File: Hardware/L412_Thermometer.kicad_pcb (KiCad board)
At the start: 2 copper layers, 45 x 45 mm, 21 parts, among them J1 USB_B_Mini, J2 Conn_01x03, J3 Conn_Si7021, J4 Conn_LCD, J5 Debug, J6 Serial, Q1 BSS84AKW, U1 AP7343D-33W5, U2 STM32L412KBTx, Y1 ABS07 [9pF, 32.768kHz]

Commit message: PCB updated
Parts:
- added C10: 100n, Capacitor_SMD:C_0603_1608Metric, F.Cu at (170.2, 105.4)
- added C8: C, Capacitor_SMD:C_0603_1608Metric, F.Cu at (139.7, 93.7)
- added C9: 100n, Capacitor_SMD:C_0603_1608Metric, F.Cu at (170.2, 93.0)
- added SW1: SW_Push, Button_Switch_THT:SW_PUSH_6mm, F.Cu at (172.5, 90.7)
- added SW2: SW_Push, Button_Switch_THT:SW_PUSH_6mm, F.Cu at (172.5, 103.2)
- J1: moved to B.Cu
- J2: value Conn_01x03 -> Power
- J3: value Conn_Si7021 -> Si7021
- J4, J5: moved to F.Cu
- moved J3 47.2 mm to (172.1, 84.5), turned to 90 degrees
- moved J2 39.4 mm to (131.8, 83.8), turned to 180 degrees
- moved J6 28.6 mm to (131.8, 100.1), turned to 180 degrees
- moved C4 27.4 mm to (135.6, 83.1), turned to -90 degrees
- moved U1 25.5 mm to (138.2, 83.4), turned to -90 degrees
- moved C5 25.4 mm to (140.7, 83.1), turned to -90 degrees
- moved J4 18.0 mm to (154.7, 113.1)
- moved J1 16.6 mm to (177.7, 76.7), turned to -90 degrees
- moved C3 15.9 mm to (144.5, 85.8)
- moved R1 13.0 mm to (152.1, 108.2), turned to 90 degrees
- moved J5 5.57 mm to (151.9, 76.5)
- moved C1 5.48 mm to (146.1, 85.9)
- moved U2 5.43 mm to (150.6, 90.7)
- moved C2 5.39 mm to (155.2, 95.5)
- moved C6 5.29 mm to (140.4, 88.4)
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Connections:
- Q1 pad 1: BAT_MEAS -> BAT_MEAS_EN
- R2 pad 2: BAT_MEAS -> BAT_MEAS_EN
- R3 pad 2: VBAT -> V_BAT
- R4 pad 1: VBAT -> V_BAT
- U2 pad 29: unconnected-(U2-Pad29) -> BAT_MEAS_EN
- U2 pad 30: unconnected-(U2-Pad30) -> SCREEN
- U2 pad 6: VBAT -> WKUP
- U2 pad 7: BAT_MEAS -> V_BAT
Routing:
- net +3V3: track 61.8 -> 0.00 mm, vias 1 -> 0
- net +BATT: track 40.6 -> 0.00 mm, vias 1 -> 0
- net Net-(J3-Pad4): track 29.3 -> 0.00 mm, vias 1 -> 0
- net Net-(J3-Pad3): track 27.4 -> 0.00 mm, vias 1 -> 0
- net NRST: track 24.6 -> 0.00 mm, vias 1 -> 0
- net LCD_CE: track 23.0 -> 0.00 mm, vias 1 -> 0
- net LCD_RST: track 21.7 -> 0.00 mm
- net LCD_DC: track 21.1 -> 0.00 mm, vias 1 -> 0
- net USART_RX: track 20.8 -> 0.00 mm, vias 1 -> 0
- net USART_TX: track 20.5 -> 0.00 mm, vias 1 -> 0
- net LCD_DIN: track 19.7 -> 0.00 mm
- net LCD_CLK: track 19.5 -> 0.00 mm
- net +5V: track 17.9 -> 0.00 mm, vias 1 -> 0
- net LCD_LIGHT: track 17.4 -> 0.00 mm, vias 2 -> 0
- net SWDIO: track 15.3 -> 0.00 mm, vias 1 -> 0
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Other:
- board size 45 x 45 mm -> 60 x 45 mm

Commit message: Routed PCB
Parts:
- added C11: 4u7, Capacitor_Tantalum_SMD:CP_EIA-1608-10_AVX-L, F.Cu at (129.3, 79.1)
- added R5: 62R, Resistor_SMD:R_0603_1608Metric, B.Cu at (152.9, 84.5)
- added R6: 62R, Resistor_SMD:R_0603_1608Metric, B.Cu at (154.4, 84.5)
- added R7: 62R, Resistor_SMD:R_0603_1608Metric, B.Cu at (156.0, 84.5)
- added REF**: MountingHole_2.5mm, MountingHole:MountingHole_2.5mm, F.Cu at (125.3, 113.2)
- added REF**: MountingHole_2.5mm, MountingHole:MountingHole_2.5mm, F.Cu at (166.0, 113.2)
- added REF**: MountingHole_2.5mm, MountingHole:MountingHole_2.5mm, F.Cu at (125.3, 72.5)
- added REF**: MountingHole_2.5mm, MountingHole:MountingHole_2.5mm, F.Cu at (166.0, 72.5)
- C1, C3, J2, J3, J5, J6: moved to B.Cu
- J1: moved to F.Cu
- SW1, SW2: footprint Button_Switch_THT:SW_PUSH_6mm -> Button_Switch_SMD:SW_SPST_SKQG_WithStem
- U1: value AP7343D-33W5 -> ?
- moved J5 7.95 mm to (159.5, 78.7)
- moved J3 7.62 mm to (179.7, 84.5)
- moved C1 5.10 mm to (148.3, 90.4), turned to 0 degrees
- moved C3 4.91 mm to (148.3, 88.9), turned to 0 degrees
- moved SW2 4.40 mm to (175.8, 106.1), turned to 180 degrees
- moved C8 4.32 mm to (144.0, 93.9)
- moved SW1 3.25 mm to (175.8, 90.7)
- moved R3 2.80 mm to (141.0, 93.9)
- moved C9 1.34 mm to (170.6, 91.7)
- moved Q1 1.31 mm to (139.6, 98.7)
- moved R4 1.28 mm to (142.5, 93.9)
- moved R2 1.25 mm to (141.7, 98.7)
- moved C4 1.18 mm to (135.9, 81.9), turned to 180 degrees
- moved U1 1.08 mm to (139.2, 83.1)
- moved C5 1.08 mm to (141.7, 82.7), turned to 90 degrees
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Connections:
- net +3V3 renamed +3V0
- J5 pad 2: NRST -> Net-(J5-Pad2)
- J5 pad 3: SWCLK -> Net-(J5-Pad3)
- J5 pad 4: SWDIO -> Net-(J5-Pad4)
- U2 pad 18: unconnected-(U2-Pad18) -> SCREEN
- U2 pad 30: SCREEN -> unconnected-(U2-Pad30)
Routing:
- net +3V0: track 0.00 -> 84.7 mm, vias 0 -> 4
- net +5V: track 0.00 -> 48.2 mm, vias 0 -> 1
- net WKUP: track 0.00 -> 33.9 mm, vias 0 -> 2
- net +BATT: track 0.00 -> 32.4 mm
- net SCREEN: track 0.00 -> 28.4 mm
- net LCD_RST: track 0.00 -> 25.4 mm, vias 0 -> 1
- net GND: track 0.00 -> 25.4 mm, vias 0 -> 28
- net USB_DM: track 0.00 -> 24.8 mm
- net USB_DP: track 0.00 -> 24.8 mm
- net Net-(J3-Pad3): track 0.00 -> 24.6 mm, vias 0 -> 1
- net LCD_DC: track 0.00 -> 22.0 mm, vias 0 -> 1
- net LCD_CE: track 0.00 -> 21.8 mm
- net LCD_DIN: track 0.00 -> 21.3 mm, vias 0 -> 1
- net Net-(J3-Pad4): track 0.00 -> 20.8 mm, vias 0 -> 1
- net LCD_CLK: track 0.00 -> 19.7 mm
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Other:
- board text added: "+3V"
- board text added: "+5V"
- board text added: "+BATT"
- board text added: "GND"
- board text added: "NRST"
- board text added: "RX"
- board text added: "STM32L412KBT6 Thermometer v1"
- board text added: "SWCLK"
- board text added: "SWDIO"
- board text added: "Si7021"
- board text added: "TX"

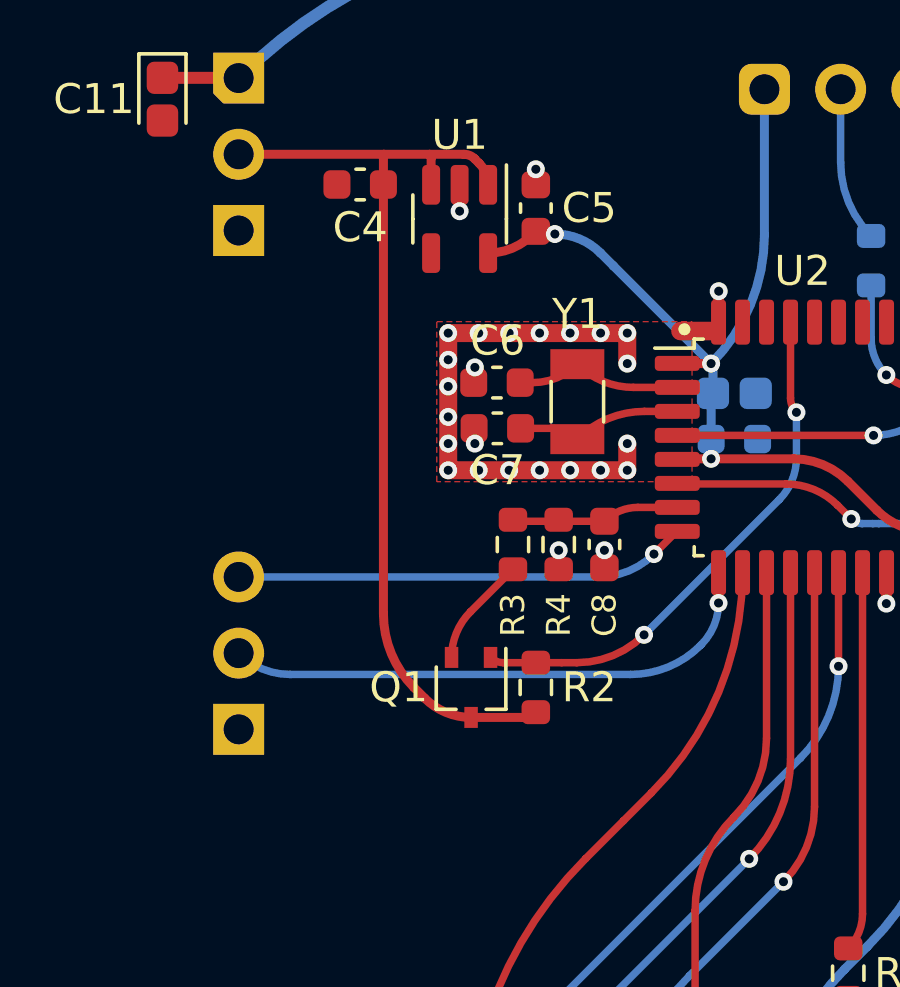
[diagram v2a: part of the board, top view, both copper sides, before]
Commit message: Voltage divider values, changed footprint of P-MOS, picked a voltage regulator
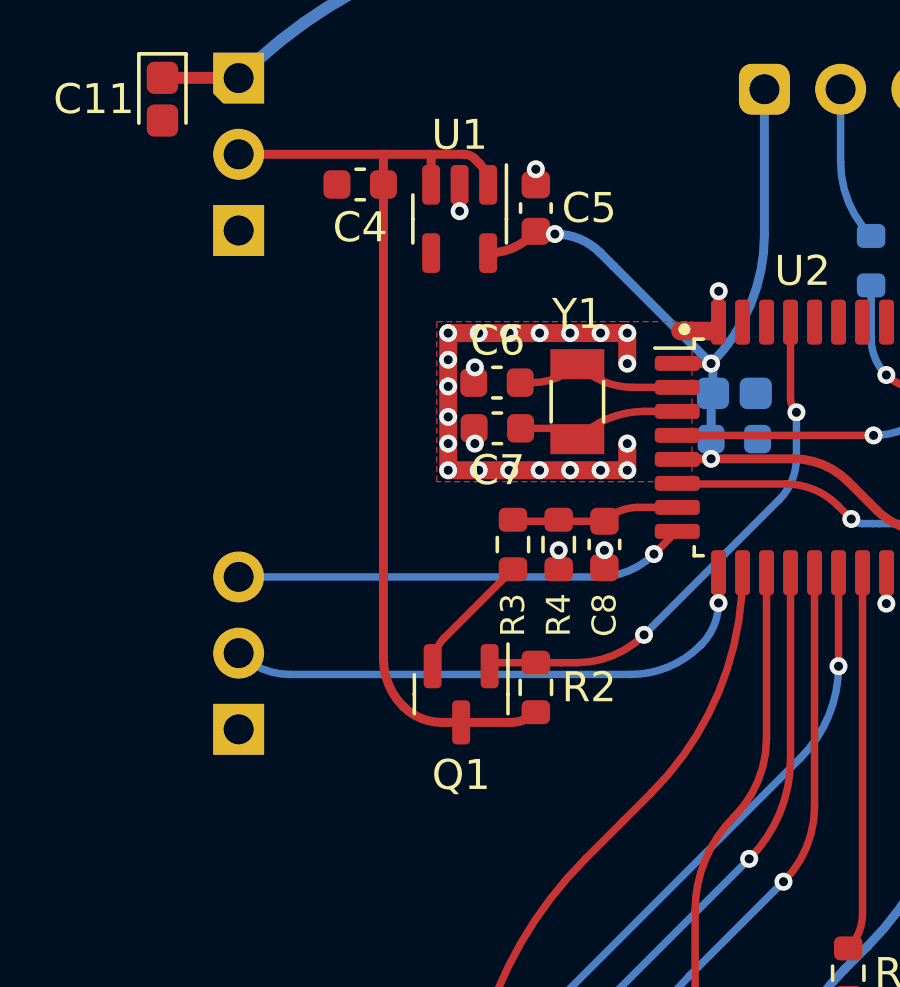
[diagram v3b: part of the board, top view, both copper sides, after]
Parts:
- Q1: value BSS84AKW -> BSS84AK; footprint Package_TO_SOT_SMD:SOT-323_SC-70 -> Package_TO_SOT_SMD:SOT-23
- R3: value R -> 10k
- R4: value R -> 30k
- U1: value ? -> MIC5317
- moved Q1 0.40 mm to (139.2, 98.9)
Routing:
- net +BATT: track 32.4 -> 33.2 mm
- net Net-(Q1-Pad2): track 3.68 -> 4.27 mm
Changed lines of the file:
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@@
       (effects (font (size 1 1) (thickness 0.15)))
     )
-    (fp_text value "?" (at 0 2.4 90) (layer "F.Fab")
+    (fp_text value "MIC5317" (at 0 2.4 90) (layer "F.Fab")
       (effects (font (size 1 1) (thickness 0.15)))
     )
@@
     (pad "" np_thru_hole circle (at 0 0) (size 2.3 2.3) (drill 2.3) (layers F&B.Cu *.Mask))
   )
-  (footprint "Package_TO_SOT_SMD:SOT-323_SC-70" (layer "F.Cu")
-    (at 139.573 98.679 -90)
-    (descr "SOT-323, SC-70")
-    (tags "SOT-323 SC-70")
-    (property "Sheetfile" "L412_Thermometer.kicad_sch")
-    (property "Sheetname" "")
-    (attr smd)
-    (fp_text reference "Q1" (at 0 2.413 180) (layer "F.SilkS")
-      (effects (font (size 1 1) (thickness 0.15)))
-    )
-    (fp_text value "BSS84AKW" (at -0.05 2.05 90) (layer "F.Fab")
-      (effects (font (size 1 1) (thickness 0.15)))
-    )
-    (fp_text user "${REFERENCE}" (at 0 0) (layer "F.Fab")
-      (effects (font (size 0.5 0.5) (thickness 0.075)))
-    )
-    (fp_line (start -0.68 1.16) (end 0.73 1.16) (layer "F.SilkS") (width 0.12))
-    (fp_line (start 0.73 -1.16) (end -1.3 -1.16) (layer "F.SilkS") (width 0.12))
-    (fp_line (start 0.73 -1.16) (end 0.73 -0.5) (layer "F.SilkS") (width 0.12))
-    (fp_line (start 0.73 0.5) (end 0.73 1.16) (layer "F.SilkS") (width 0.12))
-    (fp_line (start -1.7 -1.3) (end 1.7 -1.3) (layer "F.CrtYd") (width 0.05))
-    (fp_line (start -1.7 1.3) (end -1.7 -1.3) (layer "F.CrtYd") (width 0.05))
-    (fp_line (start 1.7 1.3) (end -1.7 1.3) (layer "F.CrtYd") (width 0.05))
-    (fp_line (start 1.7 -1.3) (end 1.7 1.3) (layer "F.CrtYd") (width 0.05))
-    (fp_line (start 0.67 1.1) (end -0.68 1.1) (layer "F.Fab") (width 0.1))
-    (fp_line (start -0.68 -0.6) (end -0.68 1.1) (layer "F.Fab") (width 0.1))
-    (fp_line (start 0.67 -1.1) (end -0.18 -1.1) (layer "F.Fab") (width 0.1))
-    (fp_line (start 0.67 -1.1) (end 0.67 1.1) (layer "F.Fab") (width 0.1))
-    (fp_line (start -0.18 -1.1) (end -0.68 -0.6) (layer "F.Fab") (width 0.1))
-    (pad "1" smd rect (at -1 -0.65 180) (size 0.45 0.7) (layers "F.Cu" "F.Paste" "F.Mask")
+  (footprint "Package_TO_SOT_SMD:SOT-23" (layer "F.Cu")
+    (at 139.2428 98.9076 -90)
+    (descr "SOT, 3 Pin (https://www.jedec.org/system/files/docs/to-236h.pdf variant AB), generated with kicad-footprint-generator ipc_gullwing_generator.py")
+    (tags "SOT TO_SOT_SMD")
+    (property "Sheetfile" "L412_Thermometer.kicad_sch")
+    (property "Sheetname" "")
+    (attr smd)
+    (fp_text reference "Q1" (at 2.6924 0) (layer "F.SilkS")
+      (effects (font (size 1 1) (thickness 0.15)))
+    )
+    (fp_text value "BSS84AK" (at 0 2.4 -90) (layer "F.Fab")
+      (effects (font (size 1 1) (thickness 0.15)))
+    )
+    (fp_text user "${REFERENCE}" (at 0 0 -90) (layer "F.Fab")
+      (effects (font (size 0.32 0.32) (thickness 0.05)))
+    )
+    (fp_line (start 0 -1.56) (end -1.675 -1.56) (layer "F.SilkS") (width 0.12))
+    (fp_line (start 0 -1.56) (end 0.65 -1.56) (layer "F.SilkS") (width 0.12))
+    (fp_line (start 0 1.56) (end -0.65 1.56) (layer "F.SilkS") (width 0.12))
+    (fp_line (start 0 1.56) (end 0.65 1.56) (layer "F.SilkS") (width 0.12))
+    (fp_line (start -1.92 1.7) (end 1.92 1.7) (layer "F.CrtYd") (width 0.05))
+    (fp_line (start 1.92 1.7) (end 1.92 -1.7) (layer "F.CrtYd") (width 0.05))
+    (fp_line (start 1.92 -1.7) (end -1.92 -1.7) (layer "F.CrtYd") (width 0.05))
+    (fp_line (start -1.92 -1.7) (end -1.92 1.7) (layer "F.CrtYd") (width 0.05))
+    (fp_line (start -0.65 -1.125) (end -0.325 -1.45) (layer "F.Fab") (width 0.1))
+    (fp_line (start 0.65 -1.45) (end 0.65 1.45) (layer "F.Fab") (width 0.1))
+    (fp_line (start -0.65 1.45) (end -0.65 -1.125) (layer "F.Fab") (width 0.1))
+    (fp_line (start 0.65 1.45) (end -0.65 1.45) (layer "F.Fab") (width 0.1))
+    (fp_line (start -0.325 -1.45) (end 0.65 -1.45) (layer "F.Fab") (width 0.1))
+    (pad "1" smd roundrect (at -0.9375 -0.95 270) (size 1.475 0.6) (layers "F.Cu" "F.Paste" "F.Mask") (roundrect_rratio 0.25)
       (net 32 "BAT_MEAS_EN") (pinfunction "G") (pintype "input"))
-    (pad "2" smd rect (at -1 0.65 180) (size 0.45 0.7) (layers "F.Cu" "F.Paste" "F.Mask")
+    (pad "2" smd roundrect (at -0.9375 0.95 270) (size 1.475 0.6) (layers "F.Cu" "F.Paste" "F.Mask") (roundrect_rratio 0.25)
       (net 31 "Net-(Q1-Pad2)") (pinfunction "S") (pintype "passive"))
-    (pad "3" smd rect (at 1 0 180) (size 0.45 0.7) (layers "F.Cu" "F.Paste" "F.Mask")
+    (pad "3" smd roundrect (at 0.9375 0 270) (size 1.475 0.6) (layers "F.Cu" "F.Paste" "F.Mask") (roundrect_rratio 0.25)
       (net 1 "+BATT") (pinfunction "D") (pintype "passive"))
-    (model "${KICAD6_3DMODEL_DIR}/Package_TO_SOT_SMD.3dshapes/SOT-323_SC-70.wrl"
+    (model "${KICAD6_3DMODEL_DIR}/Package_TO_SOT_SMD.3dshapes/SOT-23.wrl"
       (offset (xyz 0 0 0))
       (scale (xyz 1 1 1))
@@
       (effects (font (size 0.8 0.8) (thickness 0.15)))
     )
-    (fp_text value "R" (at 0 1.43 90) (layer "F.Fab")
+    (fp_text value "10k" (at 0 1.43 90) (layer "F.Fab")
       (effects (font (size 1 1) (thickness 0.15)))
     )
@@
       (effects (font (size 0.8 0.8) (thickness 0.15)))
     )
-    (fp_text value "R" (at 0 1.43 90) (layer "F.Fab")
+    (fp_text value "30k" (at 0 1.43 90) (layer "F.Fab")
       (effects (font (size 1 1) (thickness 0.15)))
     )
@@
     (effects (font (size 1 1) (thickness 0.15)) (justify left mirror))
   )
+  (segment (start 136.652 81.915) (end 136.652 97.719654) (width 0.3) (layer "F.Cu") (net 1))
   (segment (start 131.826 80.908) (end 136.667 80.908) (width 0.3) (layer "F.Cu") (net 1))
-  (segment (start 136.652 96.22616) (end 136.652 81.915) (width 0.3) (layer "F.Cu") (net 1))
-  (segment (start 139.573 99.679) (end 141.309513 99.679) (width 0.3) (layer "F.Cu") (net 1))
+  (segment (start 138.594588 99.8451) (end 139.2428 99.8451) (width 0.3) (layer "F.Cu") (net 1))
   (segment (start 136.667 80.908) (end 138.191 80.908) (width 0.3) (layer "F.Cu") (net 1))
   (segment (start 138.191 80.908) (end 139.334 80.908) (width 0.3) (layer "F.Cu") (net 1))
-  (segment (start 138.028069 99.039068) (end 137.668 98.679) (width 0.3) (layer "F.Cu") (net 1))
   (segment (start 138.242 81.926) (end 138.242 81.031124) (width 0.3) (layer "F.Cu") (net 1))
   (segment (start 139.845293 81.209686) (end 139.691822 81.056215) (width 0.3) (layer "F.Cu") (net 1))
   (segment (start 136.652 81.926) (end 136.652 80.944213) (width 0.3) (layer "F.Cu") (net 1))
-  (arc (start 141.309513 99.679) (mid 141.538161 99.633519) (end 141.732 99.504) (width 0.3) (layer "F.Cu") (net 1))
+  (segment (start 139.2428 99.8451) (end 140.908512 99.8451) (width 0.3) (layer "F.Cu") (net 1))
+  (arc (start 140.908512 99.8451) (mid 141.35418 99.756451) (end 141.732 99.504) (width 0.3) (layer "F.Cu") (net 1))
   (arc (start 139.691822 81.056215) (mid 139.527652 80.94652) (end 139.334 80.908) (width 0.3) (layer "F.Cu") (net 1))
   (arc (start 138.242 81.031124) (mid 138.228746 80.96449) (end 138.191 80.908) (width 0.3) (layer "F.Cu") (net 1))
+  (arc (start 136.652 97.719654) (mid 136.823633 98.582507) (end 137.3124 99.314) (width 0.3) (layer "F.Cu") (net 1))
   (arc (start 139.845293 81.209686) (mid 140.064888 81.538334) (end 140.142 81.926) (width 0.3) (layer "F.Cu") (net 1))
-  (arc (start 137.668 98.679) (mid 136.91605 97.553628) (end 136.652 96.22616) (width 0.3) (layer "F.Cu") (net 1))
+  (arc (start 137.3124 99.314) (mid 137.900673 99.707071) (end 138.594588 99.8451) (width 0.3) (layer "F.Cu") (net 1))
   (arc (start 136.652 80.944213) (mid 136.655898 80.924615) (end 136.667 80.908) (width 0.3) (layer "F.Cu") (net 1))
-  (arc (start 139.573 99.679) (mid 138.736889 99.512687) (end 138.028069 99.039068) (width 0.3) (layer "F.Cu") (net 1))
   (segment (start 141.211 88.519) (end 141.631259 88.519) (width 0.25) (layer "F.Cu") (net 2))
   (segment (start 146.447 88.678) (end 144.984601 88.678) (width 0.25) (layer "F.Cu") (net 2))
@@
   (arc (start 158.45533 94.19333) (mid 156.776874 93.071821) (end 154.797 92.678) (width 0.25) (layer "F.Cu") (net 30))
   (arc (start 170.55 104.267) (mid 168.682839 103.895599) (end 167.099937 102.837937) (width 0.25) (layer "F.Cu") (net 30))
-  (segment (start 139.553032 96.157968) (end 140.97 94.741) (width 0.25) (layer "F.Cu") (net 31))
-  (arc (start 138.923 97.679) (mid 139.08674 96.855823) (end 139.553032 96.157968) (width 0.25) (layer "F.Cu") (net 31))
+  (segment (start 138.683052 97.027948) (end 140.97 94.741) (width 0.25) (layer "F.Cu") (net 31))
+  (arc (start 138.2928 97.9701) (mid 138.394223 97.460211) (end 138.683052 97.027948) (width 0.25) (layer "F.Cu") (net 31))
   (segment (start 142.59349 97.854) (end 141.732 97.854) (width 0.25) (layer "F.Cu") (net 32))
-  (segment (start 141.732 97.854) (end 140.645487 97.854) (width 0.25) (layer "F.Cu") (net 32))
   (segment (start 142.59349 97.854) (end 143.099376 97.854) (width 0.25) (layer "F.Cu") (net 32))
+  (segment (start 141.732 97.854) (end 140.47309 97.854) (width 0.25) (layer "F.Cu") (net 32))
   (segment (start 150.222 89.034483) (end 150.222 86.503) (width 0.25) (layer "F.Cu") (net 32))
   (via (at 150.4188 89.5096) (size 0.6) (drill 0.3) (layers "F.Cu" "B.Cu") (net 32))
@@
   (arc (start 150.4188 89.5096) (mid 150.273146 89.291615) (end 150.222 89.034483) (width 0.25) (layer "F.Cu") (net 32))
   (arc (start 143.099376 97.854) (mid 144.311344 97.612924) (end 145.3388 96.9264) (width 0.25) (layer "F.Cu") (net 32))
-  (arc (start 140.645487 97.854) (mid 140.416839 97.808519) (end 140.223 97.679) (width 0.25) (layer "F.Cu") (net 32))
+  (arc (start 140.47309 97.854) (mid 140.321398 97.884173) (end 140.1928 97.9701) (width 0.25) (layer "F.Cu") (net 32))
   (segment (start 150.4188 91.0336) (end 150.4188 89.5096) (width 0.25) (layer "B.Cu") (net 32))
   (segment (start 145.3388 96.9264) (end 149.844063 92.421137) (width 0.25) (layer "B.Cu") (net 32))
